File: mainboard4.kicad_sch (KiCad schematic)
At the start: 10 parts, among them J13 USB_C_Receptacle_USB2.0_16P, J8 Barrel_Jack

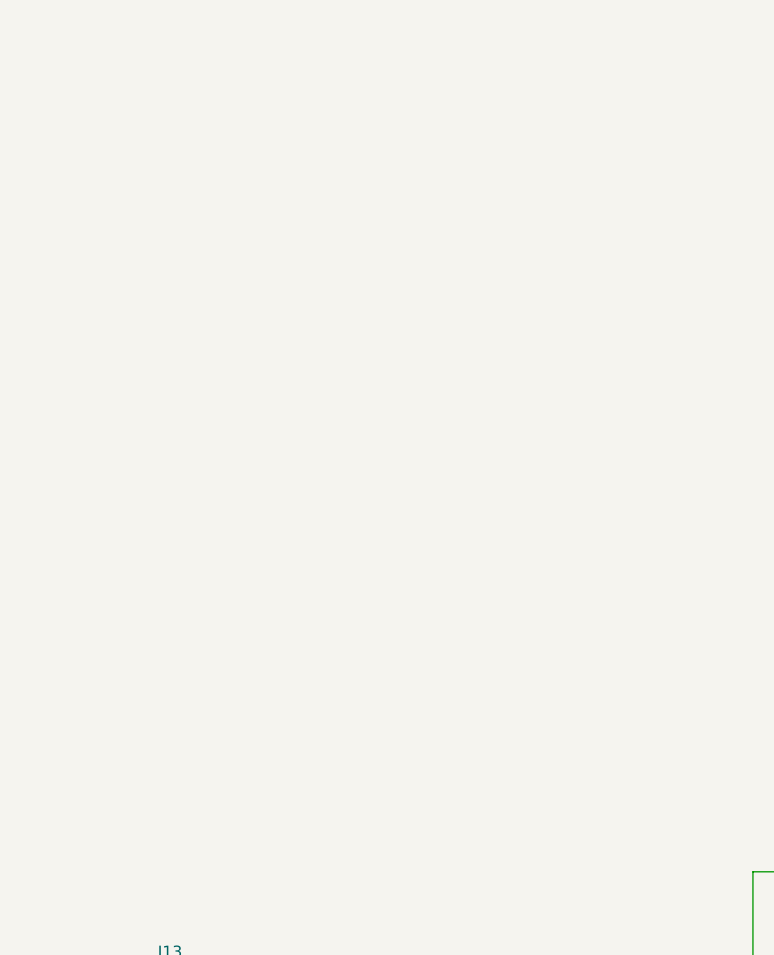
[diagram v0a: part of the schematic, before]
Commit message: add pcie root
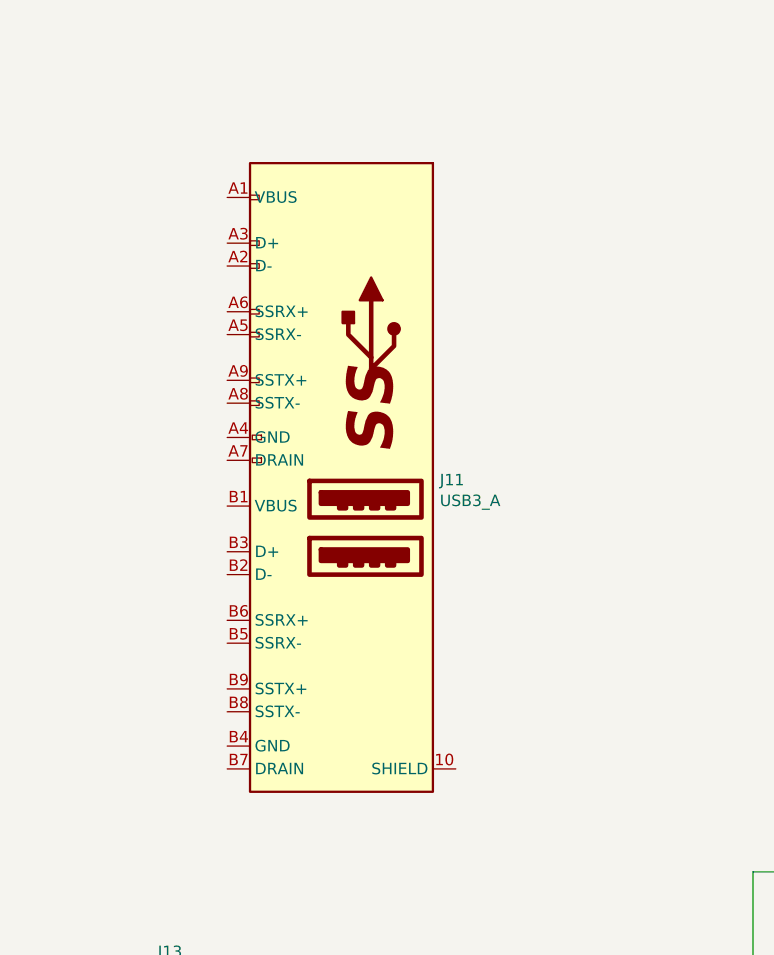
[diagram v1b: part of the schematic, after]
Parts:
- added J11: USB3_A, CM5IO:MTCONN_UBAF30-D2011, symbol CM5IO:USB3_A
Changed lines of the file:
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@@
+	)
+	(symbol
+		(lib_id "CM5IO:USB3_A")
+		(at 43.18 63.5 0)
+		(unit 1)
+		(exclude_from_sim no)
+		(in_bom yes)
+		(on_board yes)
+		(dnp no)
+		(property "Reference" "J11"
+			(at 55.372 68.2244 0)
+			(effects
+				(font
+					(size 1.27 1.27)
+				)
+				(justify left)
+			)
+		)
+		(property "Value" "USB3_A"
+			(at 55.372 70.5358 0)
+			(effects
+				(font
+					(size 1.27 1.27)
+				)
+				(justify left)
+			)
+		)
+		(property "Footprint" "CM5IO:MTCONN_UBAF30-D2011"
+			(at 46.99 43.18 0)
+			(effects
+				(font
+					(size 1.27 1.27)
+				)
+				(hide yes)
+			)
+		)
+		(property "Datasheet" "~"
+			(at 46.99 43.18 0)
+			(effects
+				(font
+					(size 1.27 1.27)
+				)
+				(hide yes)
+			)
+		)
+		(property "Description" ""
+			(at 43.18 63.5 0)
+			(effects
+				(font
+					(size 1.27 1.27)
+				)
+				(hide yes)
+			)
+		)
+		(property "Field6" "UBAF30-D2011"
+			(at 43.18 63.5 0)
+			(effects
+				(font
+					(size 1.27 1.27)
+				)
+				(hide yes)
+			)
+		)
+		(property "Field7" "Mtconn"
+			(at 43.18 63.5 0)
+			(effects
+				(font
+					(size 1.27 1.27)
+				)
+				(hide yes)
+			)
+		)
+		(property "Field5" "UBAF30-D2011"
+			(at 43.18 63.5 0)
+			(effects
+				(font
+					(size 1.27 1.27)
+				)
+				(hide yes)
+			)
+		)
+		(property "Part Description" "Dual USB 3 connector"
+			(at 43.18 63.5 0)
+			(effects
+				(font
+					(size 1.27 1.27)
+				)
+				(hide yes)
+			)
+		)
+		(pin "10"
+		)
+		(pin "A1"
+		)
+		(pin "A2"
+		)
+		(pin "A3"
+		)
+		(pin "A4"
+		)
+		(pin "A5"
+		)
+		(pin "A6"
+		)
+		(pin "A7"
+		)
+		(pin "A8"
+		)
+		(pin "A9"
+		)
+		(pin "B1"
+		)
+		(pin "B2"
+		)
+		(pin "B3"
+		)
+		(pin "B4"
+		)
+		(pin "B5"
+		)
+		(pin "B6"
+		)
+		(pin "B7"
+		)
+		(pin "B8"
+		)
+		(pin "B9"
+		)
+		(instances
+			(project "mainboard4"
+				(path "/dd07ab80-a59c-44f4-ac7d-849e21e1384e"
+					(reference "J11")
+					(unit 1)
+				)
+			)
+		)
 	)
 	(symbol

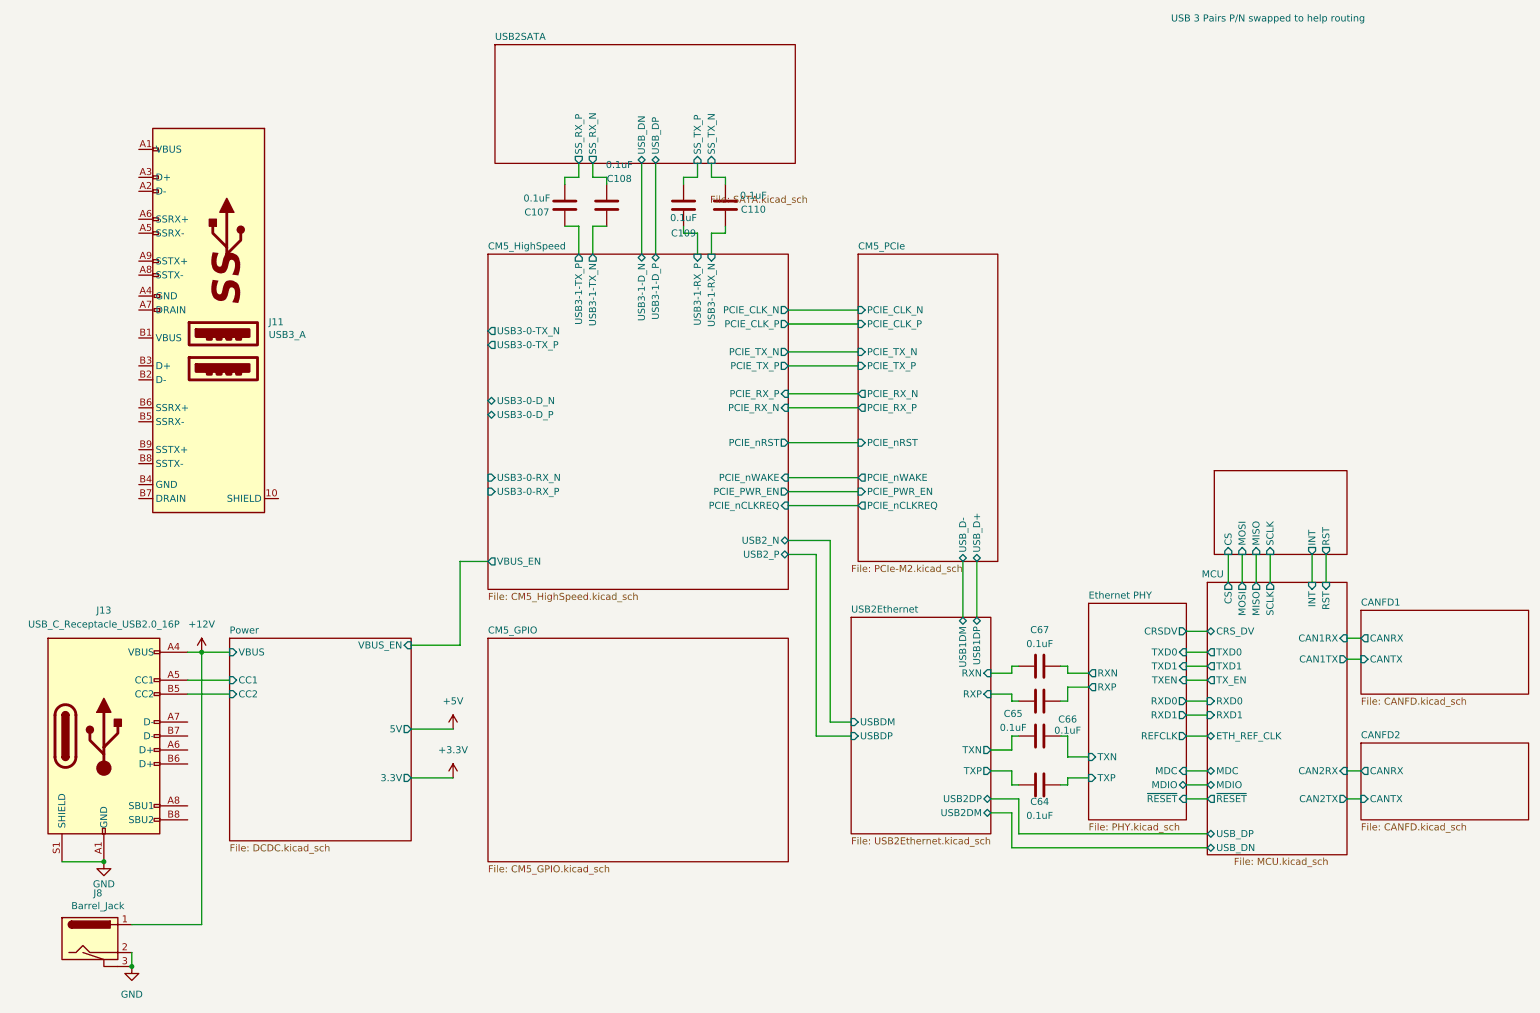
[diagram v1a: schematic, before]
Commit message: add usb3.0
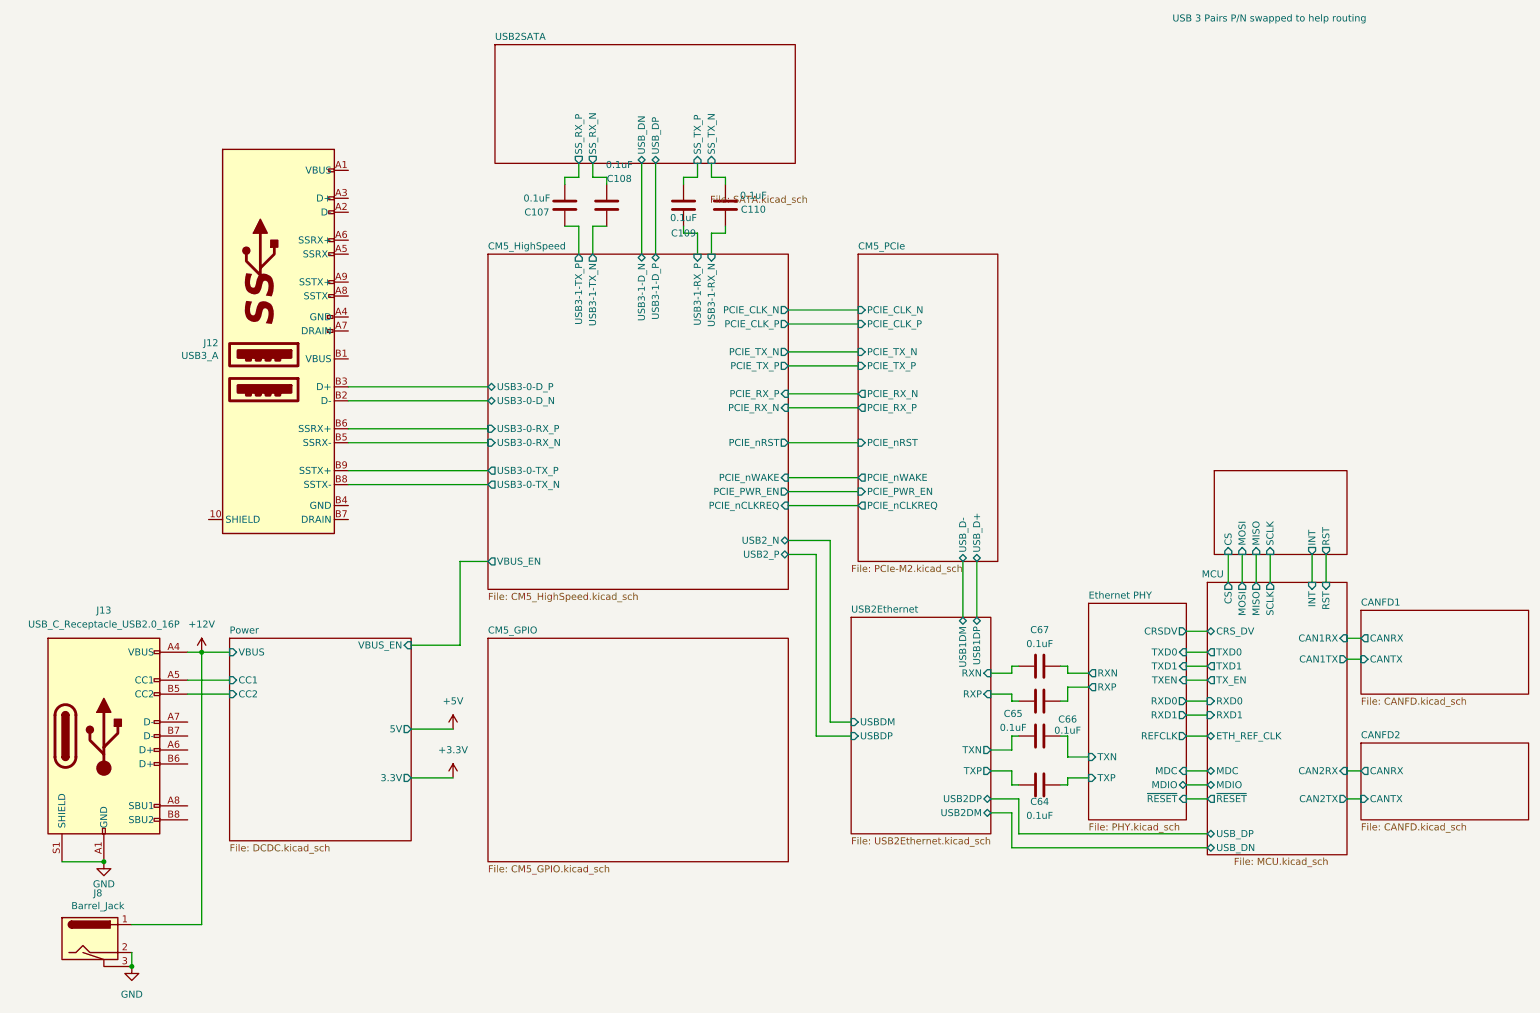
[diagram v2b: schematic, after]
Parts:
- renumbered J11 to J12
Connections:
- net CM5_HighSpeed/USB3-0-D_N: now also J12.B2 (D-)
- net CM5_HighSpeed/USB3-0-D_P: now also J12.B3 (D+)
- net CM5_HighSpeed/USB3-0-RX_N: now also J12.B5 (SSRX-)
- net CM5_HighSpeed/USB3-0-RX_P: now also J12.B6 (SSRX+)
- net CM5_HighSpeed/USB3-0-TX_N: now also J12.B8 (SSTX-)
- net CM5_HighSpeed/USB3-0-TX_P: now also J12.B9 (SSTX+)
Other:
- moved on the sheet: J12
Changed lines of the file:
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@@
+	(wire
+		(pts
+			(xy 69.85 82.55) (xy 95.25 82.55)
+		)
+		(stroke
+			(width 0)
+			(type default)
+		)
+	)
 	(wire
 		(pts
@@
 	(wire
 		(pts
+			(xy 69.85 95.25) (xy 95.25 95.25)
+		)
+		(stroke
+			(width 0)
+			(type default)
+		)
+	)
+	(wire
+		(pts
 			(xy 40.64 133.35) (xy 48.26 133.35)
 		)
@@
 	(wire
 		(pts
+			(xy 69.85 80.01) (xy 95.25 80.01)
+		)
+		(stroke
+			(width 0)
+			(type default)
+		)
+	)
+	(wire
+		(pts
 			(xy 90.17 111.76) (xy 95.25 111.76)
 		)
@@
 	(wire
 		(pts
+			(xy 69.85 97.79) (xy 95.25 97.79)
+		)
+		(stroke
+			(width 0)
+			(type default)
+		)
+	)
+	(wire
+		(pts
 			(xy 191.77 161.29) (xy 226.06 161.29)
 		)
@@
 		(pts
 			(xy 133.35 41.91) (xy 133.35 39.37)
+		)
+		(stroke
+			(width 0)
+			(type default)
+		)
+	)
+	(wire
+		(pts
+			(xy 69.85 90.17) (xy 95.25 90.17)
+		)
+		(stroke
+			(width 0)
+			(type default)
+		)
+	)
+	(wire
+		(pts
+			(xy 69.85 87.63) (xy 95.25 87.63)
 		)
 		(stroke
@@
 	(text "USB 3 Pairs P/N swapped to help routing"
 		(exclude_from_sim no)
-		(at 219.456 13.97 0)
+		(at 219.71 13.97 0)
 		(effects
 			(font
@@
 	(symbol
 		(lib_id "CM5IO:USB3_A")
-		(at 43.18 63.5 0)
+		(at 58.42 67.31 0)
+		(mirror y)
 		(unit 1)
 		(exclude_from_sim no)
@@
 		(on_board yes)
 		(dnp no)
-		(property "Reference" "J11"
-			(at 55.372 68.2244 0)
+		(property "Reference" "J12"
+			(at 46.228 72.0344 0)
 			(effects
 				(font
@@
 		)
 		(property "Value" "USB3_A"
-			(at 55.372 70.5358 0)
+			(at 46.228 74.3458 0)
 			(effects
 				(font
@@
 		)
 		(property "Footprint" "CM5IO:MTCONN_UBAF30-D2011"
-			(at 46.99 43.18 0)
+			(at 54.61 46.99 0)
 			(effects
 				(font
@@
 		)
 		(property "Datasheet" "~"
-			(at 46.99 43.18 0)
+			(at 54.61 46.99 0)
 			(effects
 				(font
@@
 		)
 		(property "Description" ""
-			(at 43.18 63.5 0)
+			(at 58.42 67.31 0)
 			(effects
 				(font
@@
 		)
 		(property "Field6" "UBAF30-D2011"
-			(at 43.18 63.5 0)
+			(at 58.42 67.31 0)
 			(effects
 				(font
@@
 		)
 		(property "Field7" "Mtconn"
-			(at 43.18 63.5 0)
+			(at 58.42 67.31 0)
 			(effects
 				(font
@@
 		)
 		(property "Field5" "UBAF30-D2011"
-			(at 43.18 63.5 0)
+			(at 58.42 67.31 0)
 			(effects
 				(font
@@
 		)
 		(property "Part Description" "Dual USB 3 connector"
-			(at 43.18 63.5 0)
+			(at 58.42 67.31 0)
 			(effects
 				(font
@@
 			(project "mainboard4"
 				(path "/dd07ab80-a59c-44f4-ac7d-849e21e1384e"
-					(reference "J11")
+					(reference "J12")
 					(unit 1)
 				)
@@
 		)
 		(pin "USB3-0-D_P" bidirectional
-			(at 95.25 85.09 180)
+			(at 95.25 80.01 180)
 			(effects
 				(font
@@
 		)
 		(pin "USB3-0-TX_P" output
-			(at 95.25 72.39 180)
+			(at 95.25 95.25 180)
 			(effects
 				(font
@@
 		)
 		(pin "USB3-0-TX_N" output
-			(at 95.25 69.85 180)
+			(at 95.25 97.79 180)
 			(effects
 				(font
@@
 		)
 		(pin "USB3-0-RX_N" input
-			(at 95.25 96.52 180)
+			(at 95.25 90.17 180)
 			(effects
 				(font
@@
 		)
 		(pin "USB3-0-RX_P" input
-			(at 95.25 99.06 180)
-			(effects
-				(font
+			(at 95.25 87.63 180)
+			(effects
+				(font

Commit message: change USB2.0
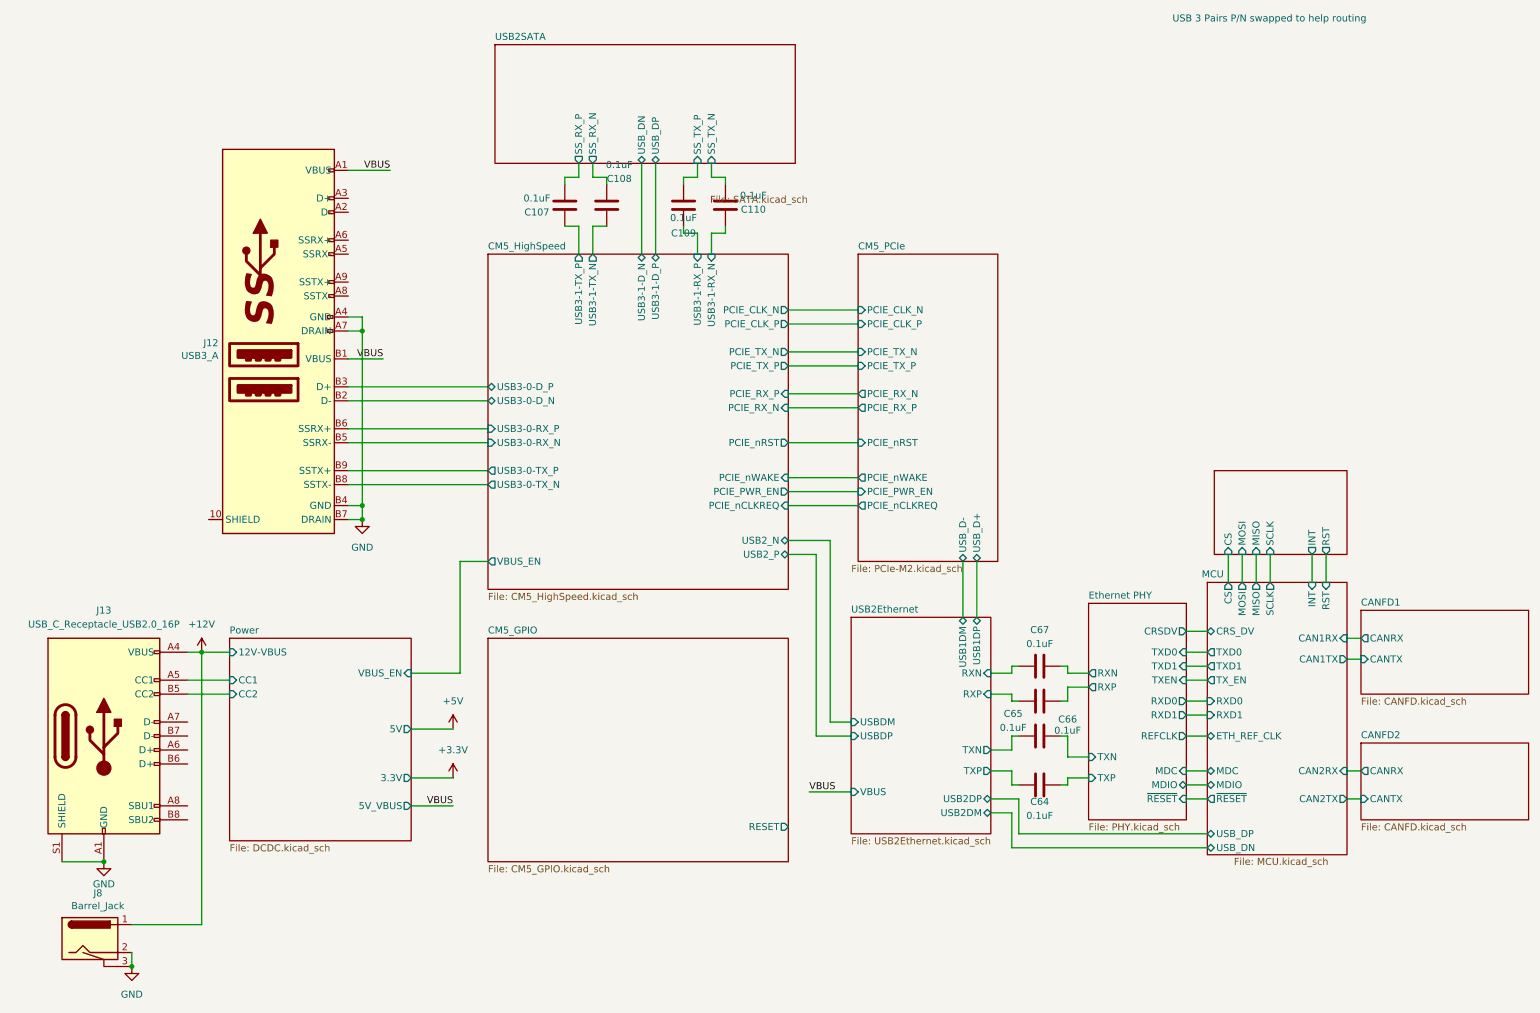
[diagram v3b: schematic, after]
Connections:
- net GND: now also J12.A4 (GND), J12.A7 (DRAIN), J12.B4 (GND), J12.B7 (DRAIN)
- net VBUS: now reaches J12.A1 (VBUS)
- net VBUS: now also J12.B1 (VBUS)
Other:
- sheet CM5_GPIO ports: added RESET; removed none
- sheet Power ports: added 12V-VBUS, 5V_VBUS; removed VBUS
- sheet USB2Ethernet ports: added VBUS; removed none

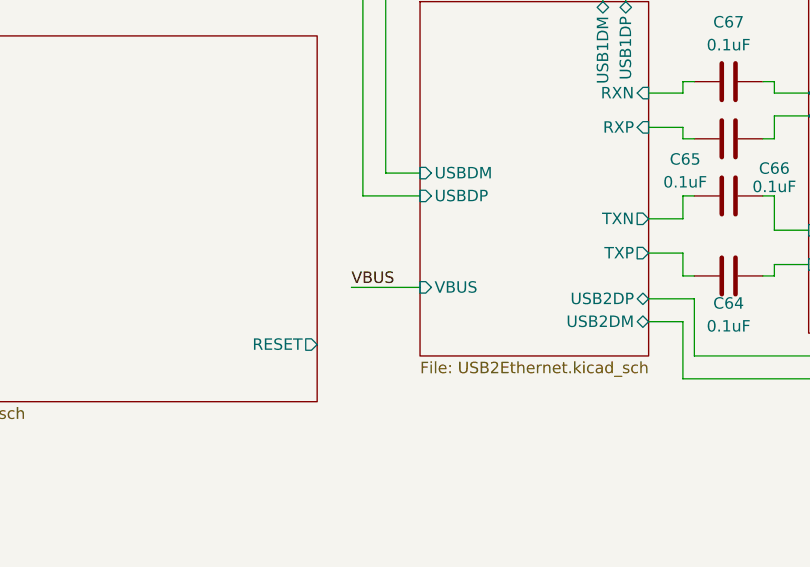
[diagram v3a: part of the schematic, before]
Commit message: add usb2.0 line
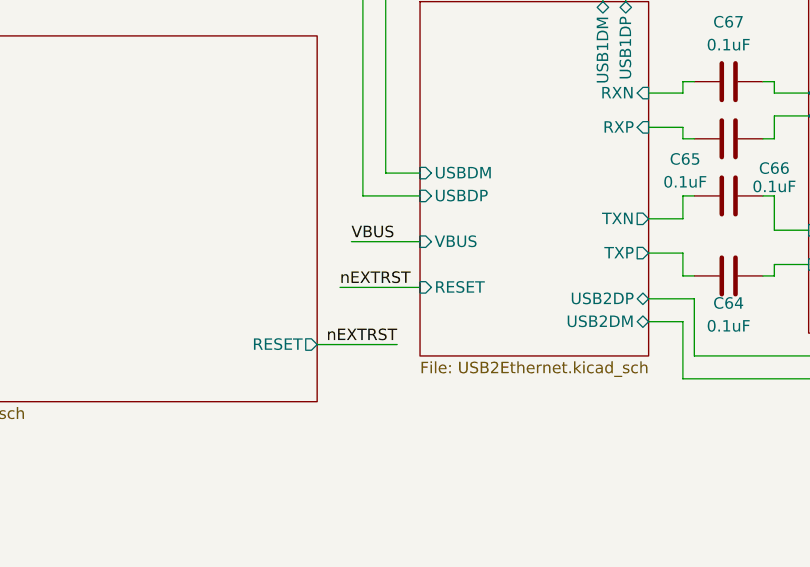
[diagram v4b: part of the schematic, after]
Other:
- sheet USB2Ethernet ports: added RESET; removed none
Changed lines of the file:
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@@
+	(wire
+		(pts
+			(xy 158.75 160.02) (xy 149.86 160.02)
+		)
+		(stroke
+			(width 0)
+			(type default)
+		)
+	)
 	(wire
 		(pts
@@
 	(wire
 		(pts
-			(xy 153.67 153.67) (xy 161.29 153.67)
+			(xy 153.67 148.59) (xy 161.29 148.59)
 		)
 		(stroke
@@
 		(pts
 			(xy 69.85 97.79) (xy 95.25 97.79)
+		)
+		(stroke
+			(width 0)
+			(type default)
+		)
+	)
+	(wire
+		(pts
+			(xy 152.4 153.67) (xy 161.29 153.67)
 		)
 		(stroke
@@
 		)
 	)
+	(label "nEXTRST"
+		(at 158.75 160.02 180)
+		(effects
+			(font
+				(size 1.27 1.27)
+			)
+			(justify right bottom)
+		)
+	)
 	(label "VBUS"
 		(at 76.2 74.93 180)
@@
 		)
 	)
+	(label "nEXTRST"
+		(at 152.4 153.67 0)
+		(effects
+			(font
+				(size 1.27 1.27)
+			)
+			(justify left bottom)
+		)
+	)
 	(label "VBUS"
-		(at 153.67 153.67 0)
+		(at 153.67 148.59 0)
 		(effects
 			(font
@@
 		)
 		(pin "VBUS" input
+			(at 161.29 148.59 180)
+			(effects
+				(font
+					(size 1.27 1.27)
+				)
+				(justify left)
+			)
+		)
+		(pin "RESET" input
 			(at 161.29 153.67 180)
 			(effects
